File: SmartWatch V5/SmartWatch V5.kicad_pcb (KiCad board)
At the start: 4 copper layers, 31.9 x 34.2 mm, 60 parts, among them J1 10118192-0001LF, J10 TestPad, J2 , J7 TestPad, J8 TestPad, J9 TestPad, Q1 FDN340P, Q2 MMBT3904, Q3 MMBT3904, Q4 FDN028N20, Q5 FDN028N20, Q6 FDN028N20, SW1 EVQ-P7J01P, SW2 EVQ-P7J01P, U1 MAX17260, U10 TSC2003IPWR, U2 FT231XQ, U3 LP5912-3.3DRVT, U5 MCP73832-2-OT, U6 ESP32-WROOM-32, U8 ADXL337

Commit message: Layout Work on Rev 5
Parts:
- removed J7: TestPad, CustomFootprints:TESTPAD
- removed R11, R12: 0, Resistor_SMD:R_0603_1608Metric
- C1, C10, C11, C2, C4, C5, C7, C8, D1, D4, J10, J2, J8, J9, Q1, Q4, Q5, Q6, R1, R13, R14, R16, R17, R18, R20, R22, R23, R24, R4, R5, R6, R7, R8, TH1, U1, U10, U3, U5, U8: moved to B.Cu
- moved R4 120.9 mm to (88.5, 91.7), turned to 90 degrees
- moved R2 116.7 mm to (93.2, 93.7), turned to 90 degrees
- moved Q1 116.2 mm to (91.0, 94.2), turned to 90 degrees
- moved R7 114.9 mm to (82.2, 93.6), turned to 270 degrees
- moved R5 114.4 mm to (90.9, 91.4)
- moved R3 112.5 mm to (95.3, 92.7), turned to 180 degrees
- moved C2 109.3 mm to (86.0, 97.2), turned to 270 degrees
- moved R19 106.6 mm to (82.9, 92.3)
- moved R10 105.9 mm to (87.4, 96.2), turned to 90 degrees
- moved C8 105.6 mm to (82.0, 97.4), turned to 270 degrees
- moved Q5 105.3 mm to (86.7, 78.0), turned to 180 degrees
- moved R21 102.0 mm to (101.7, 87.8), turned to 270 degrees
- moved R24 101.7 mm to (89.8, 75.7)
- moved C7 99.0 mm to (95.8, 93.6), turned to 90 degrees
- moved R13 97.2 mm to (95.5, 86.1), turned to 180 degrees
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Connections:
- U2 pad 17: /TXD -> /RXD0
- U6 pad 28: (no net) -> /ACCEL_EN
- U6 pad 35: /TXD0 -> /RXD
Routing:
- net /RXD0: track 0.00 -> 35.2 mm, vias 0 -> 2
- net /RXD: track 0.00 -> 31.3 mm, vias 0 -> 2
- net GND: track 2.23 -> 27.5 mm, vias 5 -> 13
- net /RTS: track 0.00 -> 13.8 mm, vias 0 -> 2
- net Net-(C3-Pad1): track 0.00 -> 13.2 mm, vias 0 -> 2
- net /VBUS: track 0.00 -> 12.1 mm, vias 0 -> 3
- net /DTR: track 0.00 -> 8.88 mm, vias 0 -> 2
- net +3V3: track 0.00 -> 7.38 mm, vias 0 -> 7
- net Net-(D3-Pad1): track 0.00 -> 7.06 mm
- net Net-(R3-Pad2): track 0.00 -> 5.30 mm
- net /BAT+: track 6.09 -> 11.2 mm
- net Net-(R2-Pad2): track 0.00 -> 4.35 mm
- net /BAT_SENSE: track 3.49 -> 6.71 mm
- net /MAX_REG: track 2.17 -> 0.00 mm
- net Net-(R8-Pad1): track 1.59 -> 0.00 mm
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- added copper zone on B.Cu, net +3V3
- added copper zone on In2.Cu, net +3V3
- added copper zone on B.Cu, net /PWR_IN
- added copper zone on In1.Cu, net GND
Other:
- board size 31.9 x 34.2 mm -> 23.7 x 34.2 mm
- net class Default: clearance 0.2 -> 0.1; trace_width 0.25 -> 0.1; via_dia 0.8 -> 0.45; via_drill 0.4 -> 0.2
- rule trace_clearance: 0.2 -> 0.1

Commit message: PCB Routing for REV5
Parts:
- removed R4: 0 (NC), Resistor_SMD:R_0603_1608Metric
- removed R5: 0, Resistor_SMD:R_0603_1608Metric
- C7, R17, R6, U5: moved to F.Cu
- moved R17 13.8 mm to (103.7, 84.9)
- moved U5 10.8 mm to (102.3, 89.6)
- moved Q4 9.76 mm to (101.2, 81.0)
- moved C7 9.41 mm to (102.4, 87.0), turned to 180 degrees
- moved R20 9.34 mm to (98.0, 82.0)
- moved TH1 8.22 mm to (103.8, 93.8)
- moved R6 7.24 mm to (101.4, 92.0), turned to 0 degrees
- moved U8 6.93 mm to (100.7, 85.0)
- moved Q5 5.45 mm to (90.2, 82.2), turned to 90 degrees
- moved R18 4.84 mm to (94.1, 94.1), turned to 90 degrees
- moved R13 4.67 mm to (95.6, 90.8), turned to 0 degrees
- moved R14 4.58 mm to (95.6, 92.0), turned to 0 degrees
- moved R24 4.22 mm to (90.1, 79.9), turned to 180 degrees
- moved R22 3.56 mm to (87.1, 79.9), turned to 180 degrees
- moved R1 3.56 mm to (94.5, 98.1)
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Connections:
- U3 pad 4: /LDO_EN -> /BAT+
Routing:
- net /EN: track 0.00 -> 54.9 mm, vias 0 -> 3
- net /REG_PG: track 1.19 -> 37.2 mm, vias 0 -> 3
- net /I2C_SCL: track 0.00 -> 29.5 mm, vias 0 -> 1
- net /I2C_SDA: track 0.00 -> 29.2 mm, vias 0 -> 1
- net /BAT_SENSE: track 6.71 -> 26.9 mm, vias 0 -> 3
- net /IO0: track 0.00 -> 18.4 mm, vias 0 -> 2
- net GND: track 27.5 -> 40.7 mm, vias 13 -> 38
- net /Y-: track 0.00 -> 8.74 mm, vias 0 -> 2
- net /X-: track 0.60 -> 9.12 mm, vias 0 -> 2
- net /X+: track 0.00 -> 6.89 mm, vias 0 -> 2
- net /Y+: track 0.00 -> 6.56 mm, vias 0 -> 2
- net Net-(D2-Pad1): track 0.00 -> 5.94 mm
- net Net-(D3-Pad1): track 7.06 -> 1.25 mm
- net +3V3: track 7.38 -> 12.5 mm, vias 7 -> 12
- net /BAT_ALRT: track 0.00 -> 5.10 mm
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- added copper zone on F.Cu, net /VBUS

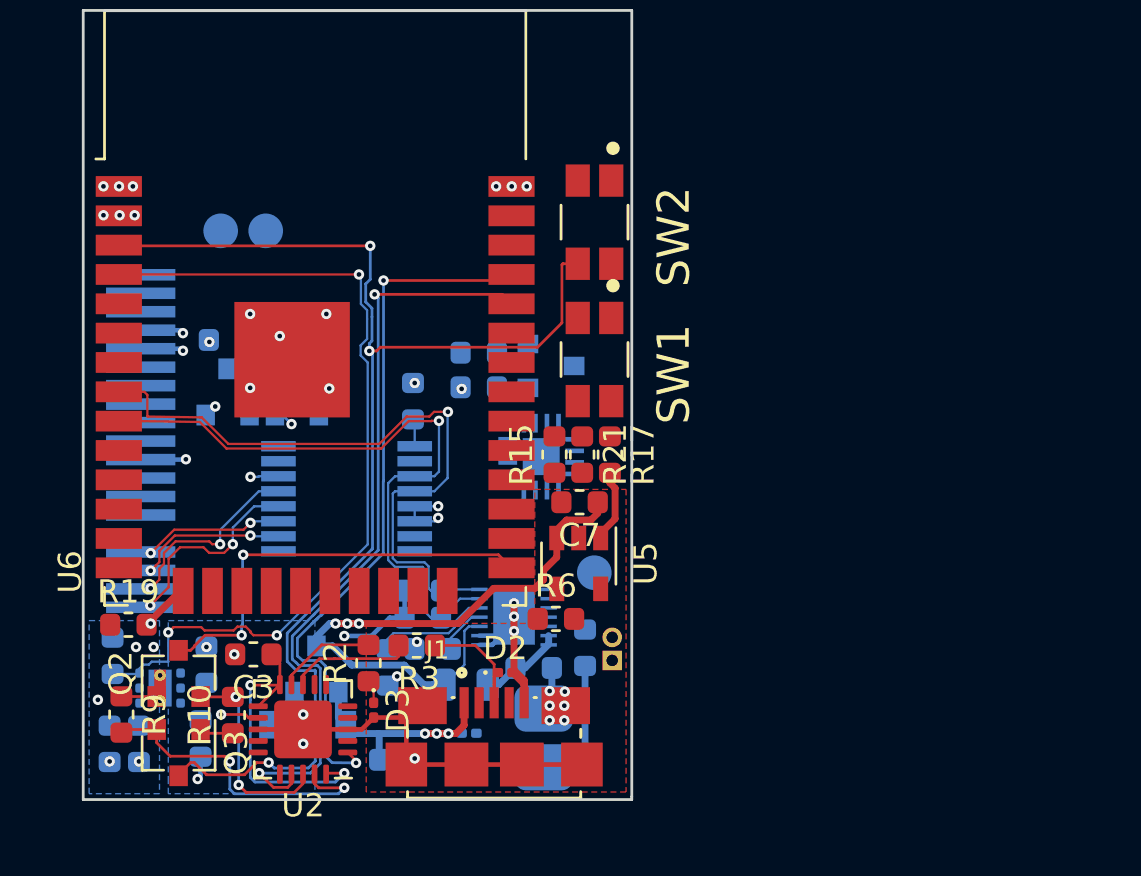
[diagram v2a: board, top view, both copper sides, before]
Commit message: Completed Rev 5 Board Layout and Routing
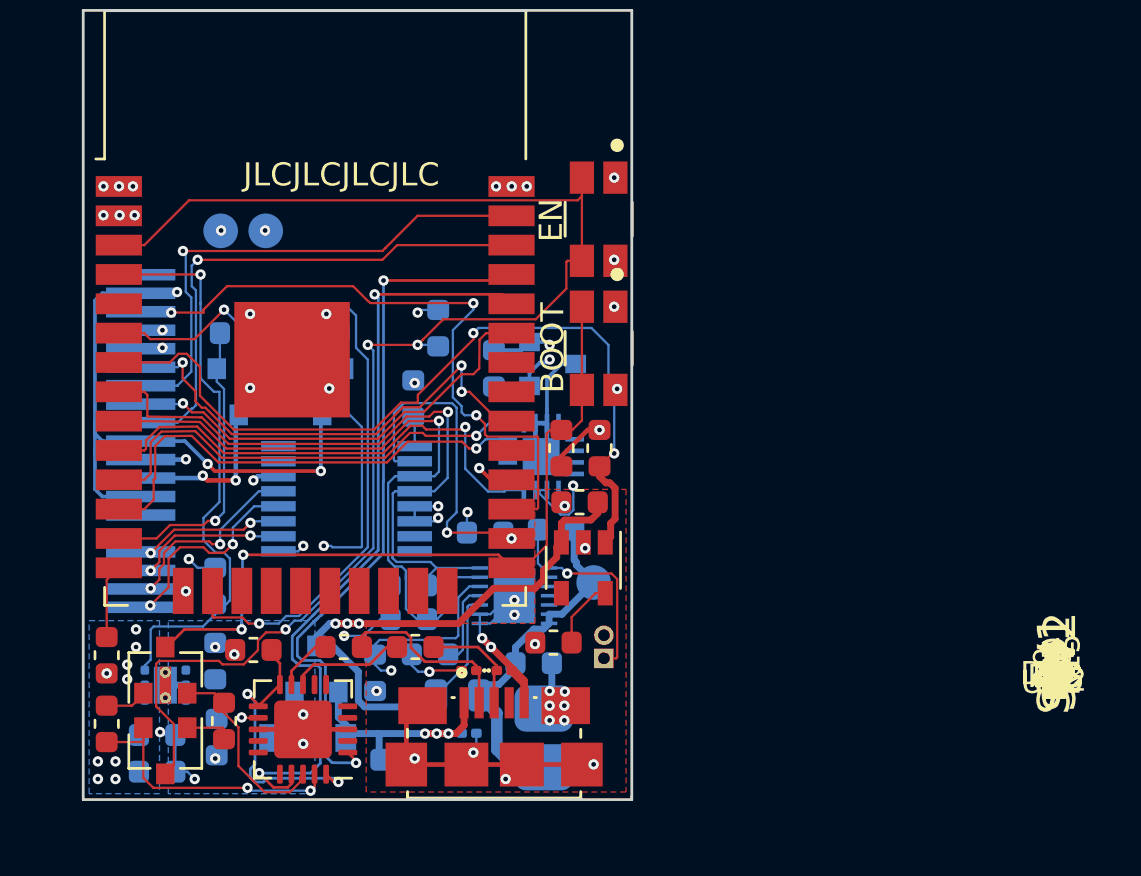
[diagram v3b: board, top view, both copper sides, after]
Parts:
- R21: moved to B.Cu
- moved R21 5.39 mm to (98.3, 88.3), turned to 0 degrees
- moved R7 5.38 mm to (86.6, 90.6)
- moved R8 5.26 mm to (101.4, 88.1), turned to 0 degrees
- moved D3 4.47 mm to (97.6, 94.2), turned to 180 degrees
- moved C8 2.39 mm to (84.1, 98.6), turned to 0 degrees
- moved R16 2.05 mm to (96.3, 79.4), turned to 270 degrees
- moved R19 1.62 mm to (81.9, 93.6), turned to 270 degrees
- moved R2 1.28 mm to (92.2, 93.2), turned to 180 degrees
- moved R24 1.12 mm to (91.2, 79.6), turned to 0 degrees
- moved Q5 1.10 mm to (91.2, 82.2), turned to 270 degrees
- moved R20 1.05 mm to (98.7, 81.2), turned to 90 degrees
- moved R6 1.03 mm to (101.3, 93.0)
- moved U1 0.93 mm to (99.6, 91.0)
- moved C5 0.87 mm to (84.1, 97.0), turned to 0 degrees
- moved R9 0.75 mm to (81.9, 96.5)
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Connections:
- U3 pad 4: /BAT+ -> /PWR_IN
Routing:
- net /CHG_STAT: track 3.18 -> 35.4 mm, vias 0 -> 2
- net /BAT_ALRT: track 5.10 -> 37.0 mm, vias 0 -> 3
- net /LCD_PWR: track 0.00 -> 28.1 mm, vias 0 -> 3
- net /LCD_CS: track 0.00 -> 27.4 mm, vias 0 -> 3
- net /LCD_EN: track 0.00 -> 24.5 mm, vias 0 -> 1
- net /LCD_RST: track 0.00 -> 23.0 mm, vias 0 -> 1
- net /LCD_MOSI: track 0.00 -> 22.7 mm, vias 0 -> 1
- net /Z_ACCEL: track 0.00 -> 21.5 mm, vias 0 -> 1
- net /LCD_SCK: track 0.00 -> 21.0 mm, vias 0 -> 3
- net /Y_ACCEL: track 0.00 -> 20.6 mm, vias 0 -> 1
- net /X_ACCEL: track 0.00 -> 20.4 mm, vias 0 -> 1
- net /LCD_A0: track 0.00 -> 19.3 mm, vias 0 -> 1
- net /TOUCH_IRQ: track 0.00 -> 14.9 mm, vias 0 -> 2
- net /IO0: track 18.4 -> 32.5 mm
- net /LCD_LED: track 0.00 -> 13.0 mm, vias 0 -> 1
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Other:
- board text added: "BOOT"
- board text added: "EN"
- board text added: "ESP32 Smartwatch Rev 5 Matthew James Bellafaire Hackady.io/Bellafaire"
- board text added: "JLCJLCJLCJLC"

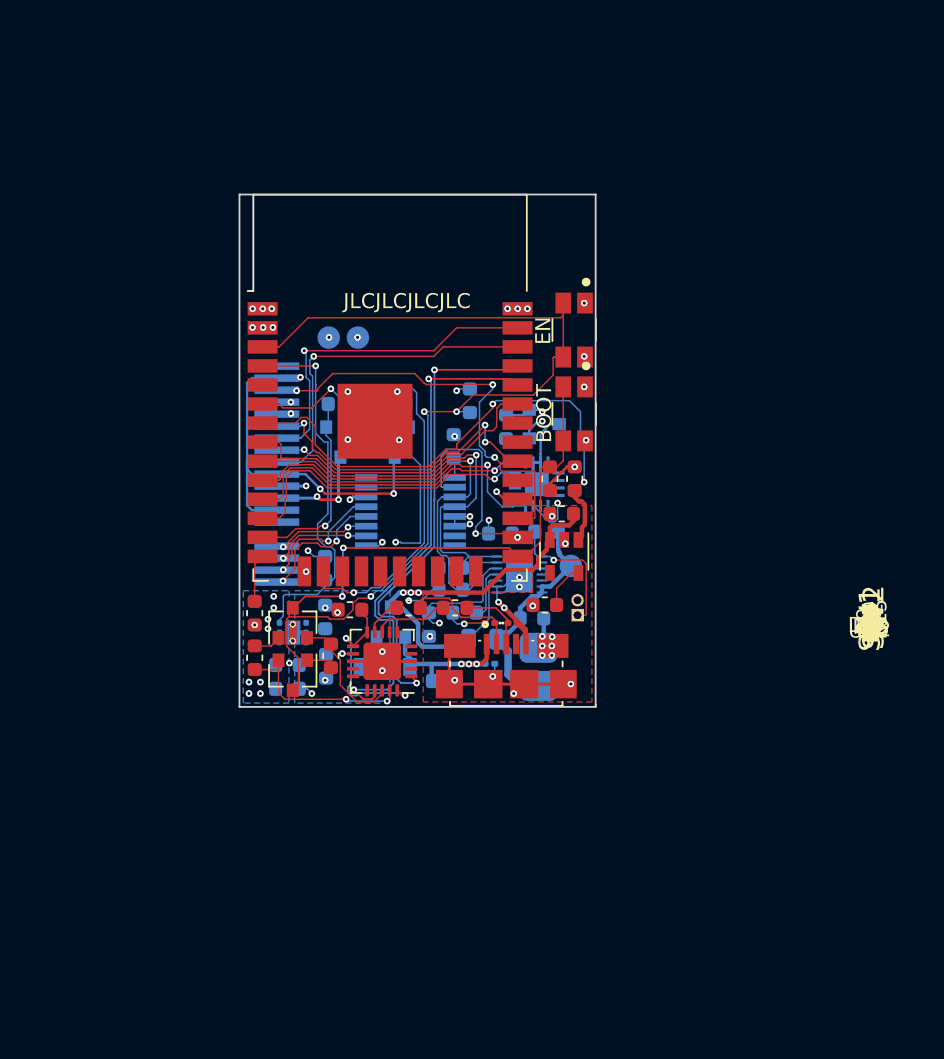
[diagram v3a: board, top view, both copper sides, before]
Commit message: Restarted Layout To Improve overall board design
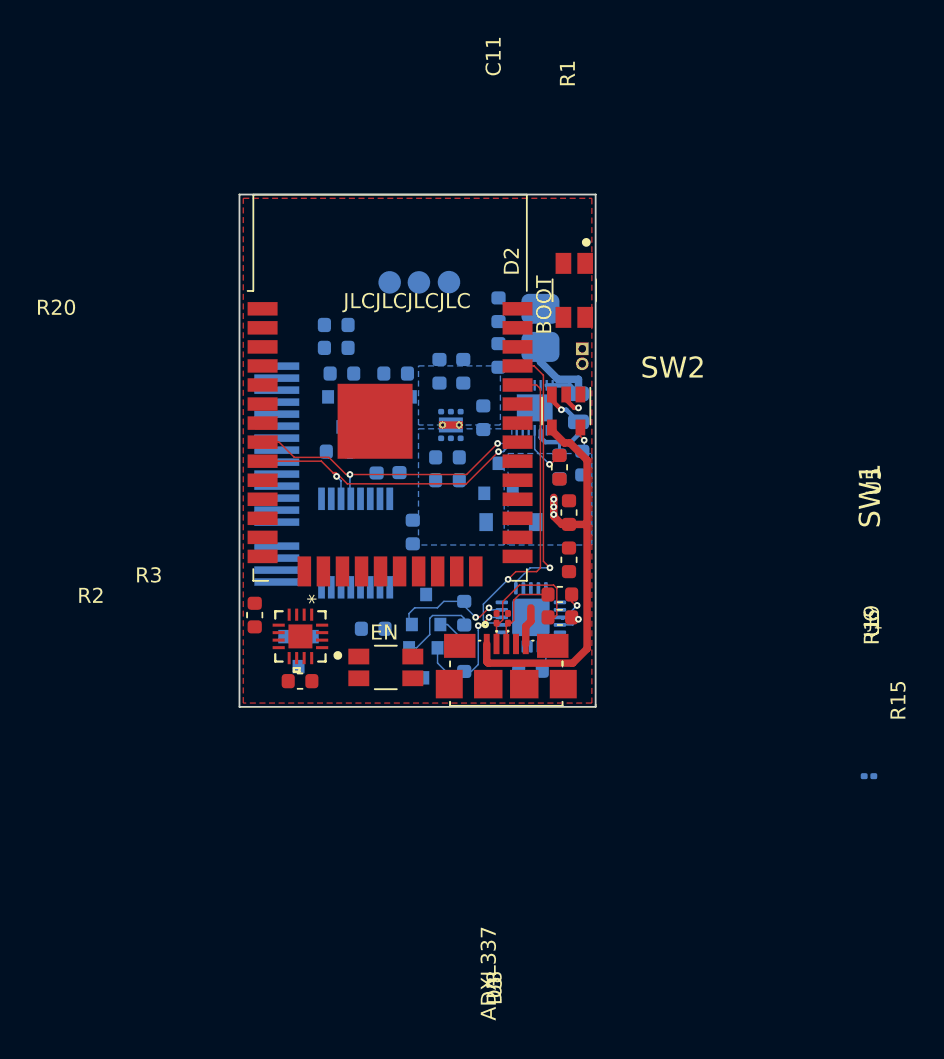
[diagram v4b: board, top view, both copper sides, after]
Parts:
- C11, R1, R20, U8: moved to F.Cu
- C3, C7, Q2, Q3, R10, R17, R6, R9, U2: moved to B.Cu
- moved D4 26.4 mm to (122.9, 104.4)
- moved SW2 25.8 mm to (90.7, 97.2), turned to 0 degrees
- moved C8 24.2 mm to (95.8, 77.4), turned to 90 degrees
- moved J2 22.6 mm to (101.0, 74.5)
- moved Q4 22.3 mm to (84.8, 96.1), turned to 270 degrees
- moved C5 22.1 mm to (94.2, 77.4), turned to 90 degrees
- moved R20 21.8 mm to (84.9, 98.1), turned to 0 degrees
- moved R18 20.9 mm to (87.4, 74.4), turned to 0 degrees
- moved C1 20.7 mm to (98.2, 73.3), turned to 90 degrees
- moved J8 20.6 mm to (94.9, 71.5)
- moved U8 18.7 mm to (85.0, 95.1), turned to 270 degrees
- moved R17 18.1 mm to (87.4, 75.9), turned to 0 degrees
- moved TH1 17.8 mm to (103.8, 75.9), turned to 180 degrees
- moved U3 17.4 mm to (95.0, 81.0), turned to 270 degrees
- moved R23 16.7 mm to (103.5, 79.9), turned to 270 degrees
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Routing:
- net /EN: track 62.9 -> 0.00 mm, vias 3 -> 0
- net GND: track 53.0 -> 3.95 mm, vias 47 -> 1
- net /BAT_ALRT: track 37.0 -> 0.00 mm, vias 3 -> 0
- net /CHG_STAT: track 35.4 -> 0.00 mm, vias 2 -> 0
- net /IO0: track 32.5 -> 0.00 mm, vias 2 -> 0
- net /LCD_PWR: track 28.1 -> 0.00 mm, vias 3 -> 0
- net /LCD_CS: track 27.4 -> 0.00 mm, vias 3 -> 0
- net /REG_PG: track 25.2 -> 0.00 mm, vias 1 -> 0
- net /LCD_EN: track 24.5 -> 0.00 mm, vias 1 -> 0
- net /LCD_RST: track 23.0 -> 0.00 mm, vias 1 -> 0
- net /LCD_MOSI: track 22.7 -> 0.00 mm, vias 1 -> 0
- net /BAT_SENSE: track 29.4 -> 7.80 mm, vias 3 -> 1
- net /Z_ACCEL: track 21.5 -> 0.00 mm, vias 1 -> 0
- net /LCD_SCK: track 21.0 -> 0.00 mm, vias 3 -> 0
- net /Y_ACCEL: track 20.6 -> 0.00 mm, vias 1 -> 0
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- added copper zone on F.Cu, net (none)
- added copper zone on In1.Cu, net +3V3
- added copper zone on B.Cu, net /VBUS
- added copper zone on In2.Cu, net GND
- removed copper zone on In2.Cu, net +3V3
- removed copper zone on F.Cu, net /VBUS
- removed copper zone on In1.Cu, net GND
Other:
- board text added: "3V3"
- board text added: "Bat"
- board text added: "GND"

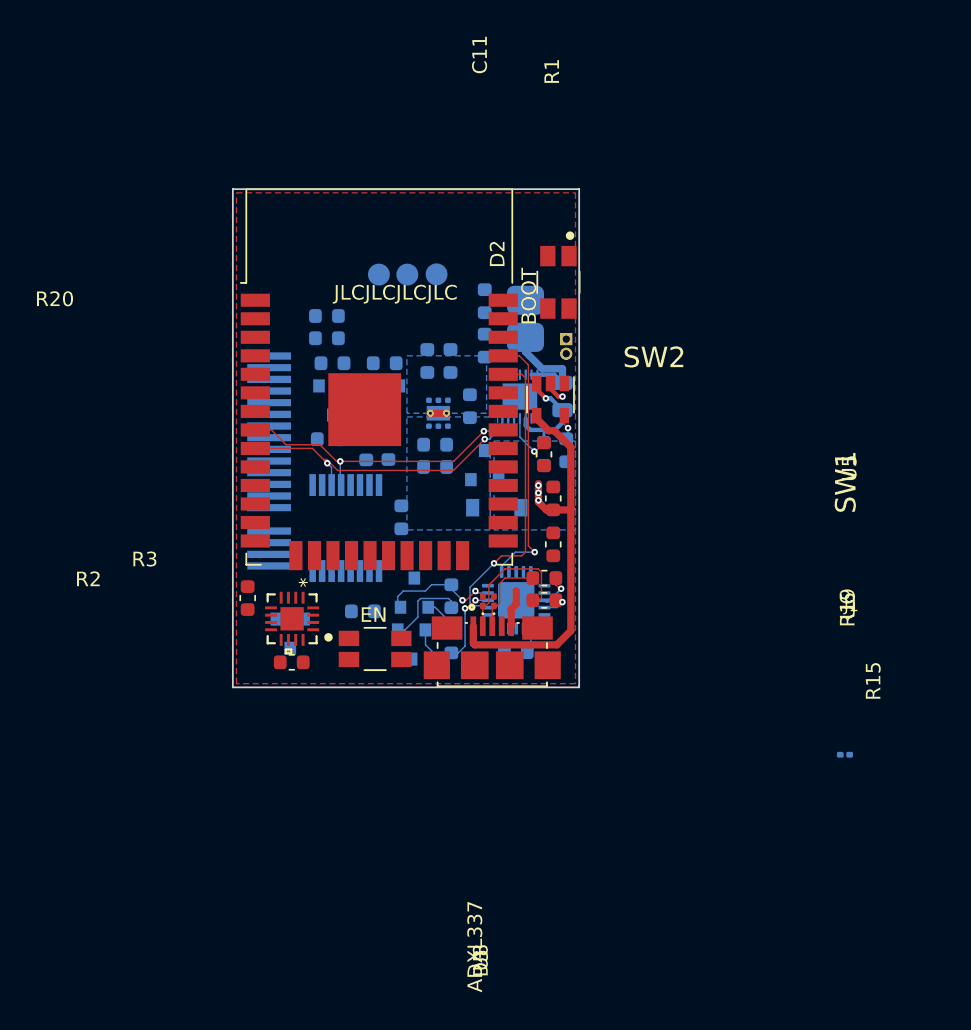
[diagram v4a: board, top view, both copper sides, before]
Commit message: Completed New Layout and Routing of Rev 5 (overall improved)
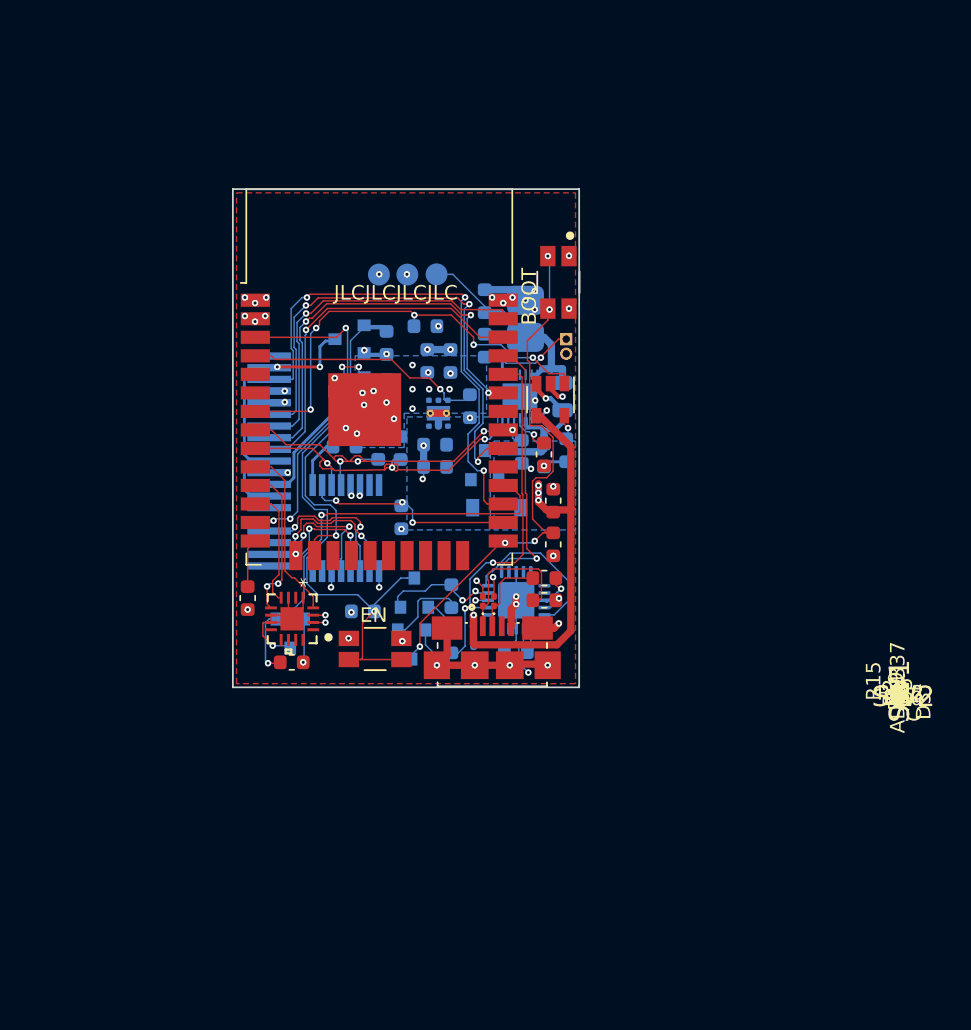
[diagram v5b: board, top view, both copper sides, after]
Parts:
- moved D4 26.4 mm to (97.4, 97.3), turned to 270 degrees
- moved R18 16.3 mm to (100.7, 83.7), turned to 90 degrees
- moved R17 6.81 mm to (94.1, 75.1), turned to 180 degrees
- moved Q5 4.88 mm to (88.9, 75.9), turned to 180 degrees
- moved R22 4.17 mm to (91.4, 79.5), turned to 270 degrees
- moved R24 1.40 mm to (91.4, 76.2), turned to 270 degrees
- moved Q6 1.32 mm to (88.9, 79.5), turned to 180 degrees
- moved C10 1.19 mm to (88.6, 83.3)
- moved R13 0.83 mm to (90.9, 83.4)
- moved R14 0.83 mm to (92.4, 83.4)
- moved R1 0.15 mm to (102.9, 87.0)
- moved C7 0.10 mm to (102.2, 83.9)
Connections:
- U6 pad 31: (no net) -> /BAT_ALRT
- U6 pad 6: /BAT_ALRT -> (no net)
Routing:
- net GND: track 3.95 -> 52.0 mm, vias 1 -> 48
- net /EN: track 0.00 -> 43.8 mm, vias 0 -> 2
- net /IO0: track 0.00 -> 37.5 mm, vias 0 -> 5
- net /LCD_CS: track 0.00 -> 36.0 mm, vias 0 -> 3
- net /LCD_SCK: track 0.00 -> 35.2 mm, vias 0 -> 3
- net /CHG_STAT: track 0.00 -> 30.7 mm, vias 0 -> 5
- net /ACCEL_EN: track 0.00 -> 29.6 mm, vias 0 -> 2
- net /LCD_A0: track 0.00 -> 29.3 mm, vias 0 -> 3
- net /LCD_RST: track 0.00 -> 24.9 mm, vias 0 -> 1
- net /LCD_MOSI: track 0.00 -> 24.5 mm, vias 0 -> 1
- net /LCD_EN: track 0.00 -> 21.7 mm, vias 0 -> 1
- net /LCD_PWR: track 0.00 -> 18.8 mm, vias 0 -> 2
- net /LCD_LED: track 0.00 -> 18.1 mm, vias 0 -> 4
- net /REG_PG: track 0.00 -> 16.4 mm, vias 0 -> 1
- net /TOUCH_IRQ: track 0.00 -> 15.0 mm, vias 0 -> 3
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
